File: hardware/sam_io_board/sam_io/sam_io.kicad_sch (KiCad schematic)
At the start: 81 parts, among them J1 Conn_01x06, J2 nmount JST 1mm QWIIC, J3 nmount SW Debug, J4 USB_C_Receptacle_USB2.0, J5 Conn_01x06, SW1 Reset, SW2 Boot, SW3 ADDRESS, U1 ADM3483, U2 W25Q128JVSIQ, U3 RP2040, U4 LMV321, U5 SN74AHCT1G125, U6 AP2112K-3.3, Y1 12MHz,18pF

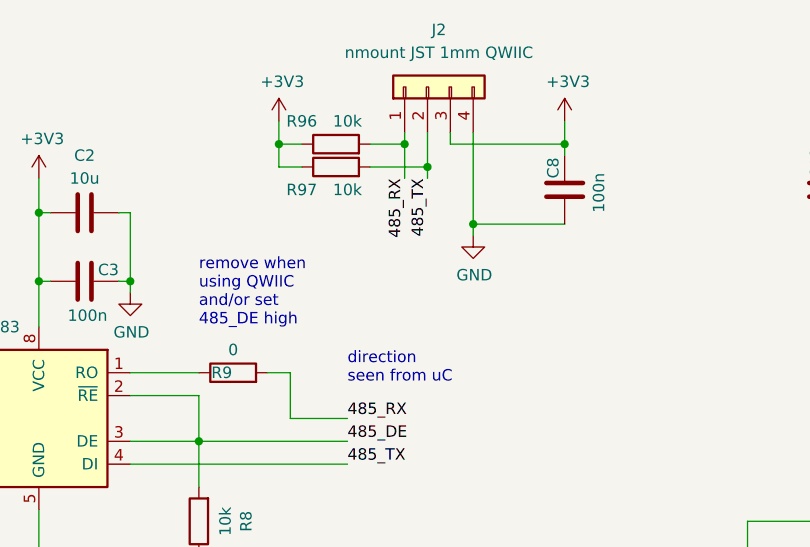
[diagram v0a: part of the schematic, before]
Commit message: SAM_IO: remove the QWIIC option (J2, R96, R97, C8); R9 becomes a track
Schematic: J2 and its pull-ups and decoupling removed, the 0 ohm R9 (U1 RO to GPIO1) replaced by a wire.
../sam_io board: the parts and their stubs removed. R9 cannot be a straight track because /485_DE runs
between its pads, so RO hops through one via on B.Cu to the existing /485_RX via. DRC: 0 unconnected,
0 clearance, schematic parity clean apart from the existing field differences.
sam_io_krt (0.15 mm) board: same removal, R9 as a straight F.Cu track, DRC unchanged.

Co-Authored-By: Claude Opus 5.5 (1M context) <noreply@anthropic.com>
Claude-Session: https://claude.ai/code/session_012ePkTGNjii74e9emvMVPmF
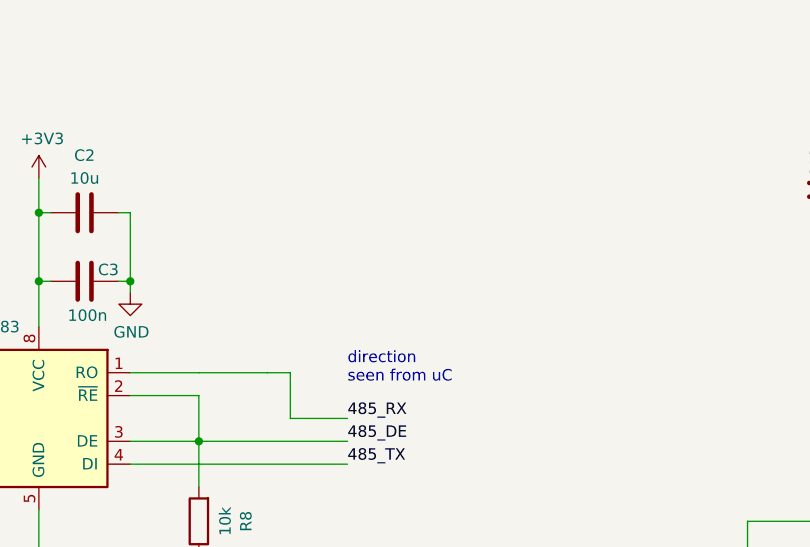
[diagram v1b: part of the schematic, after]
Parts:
- removed C8: 100n, Capacitor_SMD:C_0402_1005Metric, symbol Device:C
- removed J2: nmount JST 1mm QWIIC, Connector_JST:JST_SH_SM04B-SRSS-TB_1x04-1MP_P1.00mm_Horizontal, symbol Connector_Generic:Conn_01x04
- removed R9: 0, Resistor_SMD:R_0603_1608Metric, symbol Device:R
- removed R96, R97: 10k, Resistor_SMD:R_0603_1608Metric, symbol Device:R
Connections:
- net 485_RX: now also U1.1 (RO)
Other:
- note removed: "remove when using QWIIC and/or set 485_DE high"

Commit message: SAM_IO rev 0.2 schematic: RP2354B and SAM dedicated switch connectors
Replace the RP2040 and its W25Q flash with an RP2354B (QFN-80, internal
flash) and its switching core regulator (L1 3.3 uH, VREG_AVDD 33 R / 4.7 uF,
values as on the SAM CPU board). GPIO0-18, 25 and 29 are unchanged; the
address ladder moves to GPIO40 (ADC0).

New sheet "Dedicated switches": the SAM CPU board's harness headers J2, J3,
J13 (KK-396) with 17 input stages (1 k pull-up to 3.3 V, 10 k, 1 nF) for
J3 D9-D16, J13 D17-D24 and the coin door memory protect (J2 pin 10). The
coin slots are not routed. SWD header renamed J3 -> J20.

The PCB is not updated yet.

Co-Authored-By: Claude Opus 5.5 (1M context) <noreply@anthropic.com>
Claude-Session: https://claude.ai/code/session_01Mh8jyzQSZ4SYbwGJXqcn3P
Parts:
- removed U2: W25Q128JVSIQ, Package_SO:SOIC-8_5.23x5.23mm_P1.27mm, symbol Memory_Flash:W25Q32JVSS
- removed U3: RP2040, Package_DFN_QFN:QFN-56-1EP_7x7mm_P0.4mm_EP3.2x3.2mm, symbol MCU_RaspberryPi:RP2040
- added C34, C35, C36: 4.7u, Capacitor_SMD:C_0805_2012Metric, symbol Device:C
- added C37, C38, C39, C40, C41: 100n, Capacitor_SMD:C_0402_1005Metric, symbol Device:C
- added L1: 3.3u, Inductor_SMD:L_Cenker_CKCS201610, symbol Device:L
- added R31: 33, Resistor_SMD:R_0402_1005Metric, symbol Device:R
- added U3: RP2354B, Package_DFN_QFN:QFN-80-1EP_10x10mm_P0.4mm_EP3.4x3.4mm, symbol MCU_RaspberryPi:RP2354B
- renumbered J3 to J20
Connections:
- net +3V3: now also C35.1, C37.1, C38.1, C39.1, C40.1, R31.1, U3.15 (IOVDD), U3.24 (IOVDD), U3.29 (IOVDD), U3.41 (IOVDD), U3.5 (IOVDD), U3.50 (IOVDD), U3.60 (IOVDD), U3.64 (VREG_VIN), U3.68 (USB_OTP_VDD), U3.69 (QSPI_IOVDD), U3.76 (IOVDD)
- net 1V1: now also C36.1, C41.1, L1.2, U3.10 (DVDD), U3.32 (DVDD), U3.51 (DVDD), U3.65 (VREG_FB)
- net 3V3A: now also U3.59 (ADC_AVDD)
- net 485_DE: now also U3.79 (GPIO2)
- net 485_RX: now also U3.78 (GPIO1)
- net 485_TX: now also U3.77 (GPIO0)
- net BUS_A0: now also U3.9 (GPIO11)
- net BUS_A1: now also U3.11 (GPIO12)
- net BUS_A2: now also U3.12 (GPIO13)
- net BUS_A3: now also U3.13 (GPIO14)
- net BUS_D0: now also U3.80 (GPIO3)
- net BUS_D1: now also U3.1 (GPIO4)
- net BUS_D2: now also U3.2 (GPIO5)
- net BUS_D3: now also U3.3 (GPIO6)
- net BUS_D4: now also U3.4 (GPIO7)
- net BUS_D5: now also U3.6 (GPIO8)
- net BUS_D6: now also U3.7 (GPIO9)
- net BUS_D7: now also U3.8 (GPIO10)
- net BUS_DIR: now also U3.16 (GPIO16)
- net BUS_IOSTB: now also U3.14 (GPIO15)
- net BUS_OE_N: now also U3.17 (GPIO17)
- net GND: now also C34.2, C35.2, C36.2, C37.2, C38.2, C39.2, C40.2, C41.2, U3.62 (VREG_PGND), U3.81 (GND)
- net NBRESET_DRV: now also U3.18 (GPIO18)
- net Out_Special: now also U3.37 (GPIO29)
- net Q_nCS: now also U3.75 (~{QSPI_SS})
- net V_addr: now also U3.49 (GPIO40/ADC0)
- net nReset: now also U3.35 (RUN)
- net USB_DM_MCU: now reaches R11.2
- net USB_DM_MCU: now also U3.66 (USB_DM)
- net XIN: now reaches C6.2, Y1.3
- net XIN: now also U3.30 (XIN)
- net SWCLK: now reaches J20.1 (Pin_1)
- net SWCLK: now also U3.33 (SWCLK)
- net SWDIO: now reaches J20.3 (Pin_3)
- net SWDIO: now also U3.34 (SWDIO)
- net XOUT: now reaches R12.2
- net XOUT: now also U3.31 (XOUT)
- net at R21.1: now also U3.26 (GPIO25)
- net USB_DP_MCU: now reaches R10.2
- net USB_DP_MCU: now also U3.67 (USB_DP)
- new net DED_D10: U3.39 (GPIO31)
- new net DED_D11: U3.40 (GPIO32)
- new net DED_D12: U3.42 (GPIO33)
- new net DED_D13: U3.43 (GPIO34)
- new net DED_D14: U3.44 (GPIO35)
- new net DED_D15: U3.45 (GPIO36)
- new net DED_D16: U3.46 (GPIO37)
- new net DED_D17: U3.19 (GPIO19)
- new net DED_D18: U3.20 (GPIO20)
- new net DED_D19: U3.21 (GPIO21)
- new net DED_D20: U3.22 (GPIO22)
- new net DED_D21: U3.23 (GPIO23)
- new net DED_D22: U3.25 (GPIO24)
- new net DED_D23: U3.27 (GPIO26)
- new net DED_D24: U3.28 (GPIO27)
- new net DED_D9: U3.38 (GPIO30)
- new net MEM_PROTECT: U3.47 (GPIO38)
- new net VREG_AVDD: C34.1, R31.2, U3.61 (VREG_AVDD)
- new net VREG_LX: L1.1, U3.63 (VREG_LX)
- no-connect marks 10 -> 16
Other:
- added sheet Dedicated switches (dedicated_sw.kicad_sch)
- note added: "RP2354B core supply (RP2350 switching regulator, values as on the SAM CPU board): L1 3.3 uH from VREG_LX to DVDD (1V1), C36 4.7 uF output cap, VREG_FB to DVDD. VREG_AVDD through R31 33 R with C34 4.7 uF. Keep L1/C36/C35 tight to the chip."
- note added: "SAM_IO, derived from PPUC IO_16_8_1 v1.1.1 (TAPR OHL 1.0, see ../README.md): - IN16 (16 inputs, J6-J8) and OUT8 (8 high-power outputs, J9-J11, F2, C56) removed. - MCU is an RP2354B (2 MB internal flash, QFN-80); the RP2040 and the W25Q flash are gone. QSPI pins unused, QSPI_SS kept for BOOTSEL. - GPIO3-18 drive the SAM bus through level shifters on sheet 'SAM bus' (J9 to the SAM IO board J1). - G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"
- note removed: "SAM_IO, derived from PPUC IO_16_8_1 v1.1.1 (TAPR OHL 1.0, see ../README.md): - IN16 (16 inputs, J6-J8) and OUT8 (8 high-power outputs, J9-J11, F2, C56) removed. - GPIO3-18 drive the SAM bus through level shifters on sheet 'SAM bus' (J9 to the SAM IO board J1). - GPIO19-24, 26, 27 (former Out_1-Out_8) unused. - GPIO25 LED, GPIO28 board id and GPIO29 special output unchanged."
- moved on the sheet: C11, R13, R14, R16, R17, R18, R19, R20, R22, R23, SW3, U4
